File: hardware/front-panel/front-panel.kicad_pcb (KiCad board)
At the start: 2 copper layers, 71.1 x 128.9 mm, 0 parts

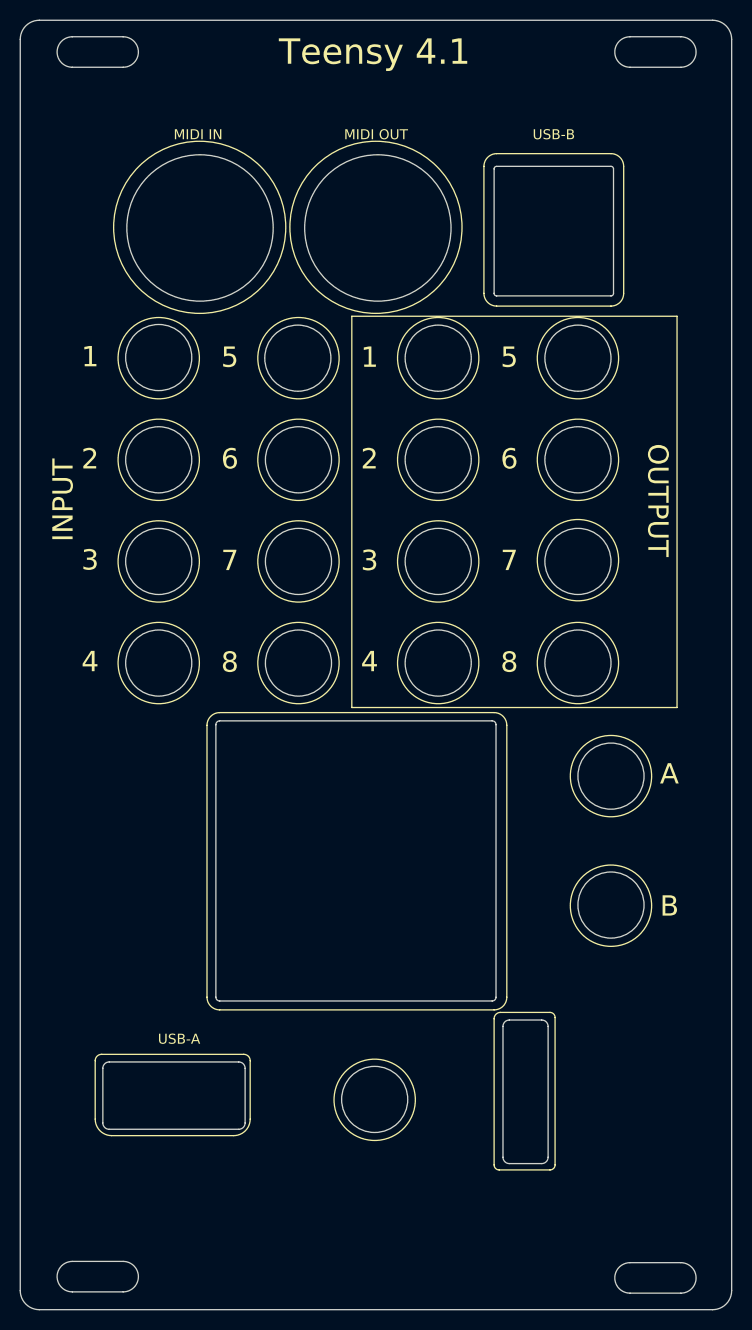
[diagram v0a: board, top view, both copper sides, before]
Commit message: schematic: fix ad7606 pin 8 (range select) from tied to gnd via res, to tied to 3v3 via resistor
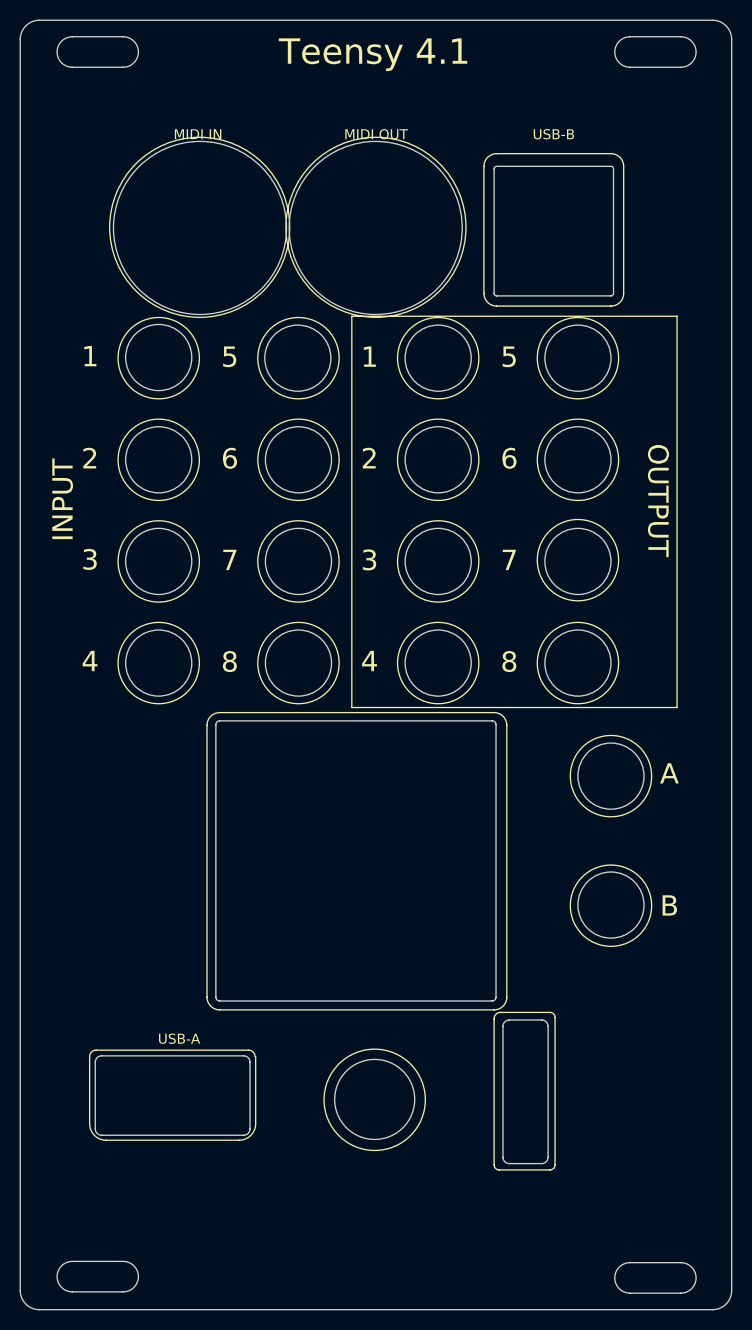
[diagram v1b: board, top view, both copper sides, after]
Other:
- outline, holes or cut-outs redrawn
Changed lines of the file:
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@@
     (uvia_drill 0.1)
   )
-  (gr_poly (pts (xy 77.724 82.042) (xy 45.212 82.042) (xy 45.212 42.926) (xy 77.724 42.926)) (layer F.Mask) (width 0.1))
+  (gr_poly (pts (xy 77.724 82.042) (xy 45.212 82.042) (xy 45.212 61.4) (xy 45.212 42.926) (xy 77.724 42.926)) (layer F.Mask) (width 0.1))
   (gr_line (start 77.724 82.042) (end 77.724 42.926) (layer F.SilkS) (width 0.12))
   (gr_line (start 45.212 82.042) (end 77.724 82.042) (layer F.SilkS) (width 0.12))
@@
   (gr_line (start 60.071 112.522) (end 65.024 112.522) (layer F.SilkS) (width 0.12))
   (gr_line (start 59.436 127.762) (end 59.436 113.157) (layer F.SilkS) (width 0.12))
-  (gr_arc (start 34.417 117.348) (end 35.052 117.348) (angle -90) (layer F.SilkS) (width 0.12))
-  (gr_arc (start 20.193 117.348) (end 20.193 116.713) (angle -90) (layer F.SilkS) (width 0.12))
-  (gr_arc (start 21.209 123.19) (end 19.558 123.19) (angle -90) (layer F.SilkS) (width 0.12))
-  (gr_arc (start 33.401 123.19) (end 33.401 124.841) (angle -90) (layer F.SilkS) (width 0.12))
-  (gr_line (start 21.209 124.841) (end 33.401 124.841) (layer F.SilkS) (width 0.12))
-  (gr_line (start 35.052 123.19) (end 35.052 117.348) (layer F.SilkS) (width 0.12))
-  (gr_line (start 19.558 123.19) (end 19.558 117.348) (layer F.SilkS) (width 0.12))
-  (gr_line (start 20.193 116.713) (end 34.417 116.713) (layer F.SilkS) (width 0.12))
-  (gr_circle (center 47.498 121.2596) (end 51.562 121.2596) (layer F.SilkS) (width 0.12))
+  (gr_arc (start 34.9 116.935) (end 35.535 116.935) (angle -90) (layer F.SilkS) (width 0.12))
+  (gr_arc (start 19.635 116.935) (end 19.635 116.3) (angle -90) (layer F.SilkS) (width 0.12))
+  (gr_arc (start 20.651 123.649) (end 19 123.649) (angle -90) (layer F.SilkS) (width 0.12))
+  (gr_arc (start 33.949 123.649) (end 33.949 125.3) (angle -90) (layer F.SilkS) (width 0.12))
+  (gr_line (start 20.651 125.3) (end 33.949 125.3) (layer F.SilkS) (width 0.12))
+  (gr_line (start 35.6 123.649) (end 35.6 116.935) (layer F.SilkS) (width 0.12))
+  (gr_line (start 19 123.649) (end 19 116.935) (layer F.SilkS) (width 0.12))
+  (gr_line (start 19.635 116.3) (end 34.9 116.3) (layer F.SilkS) (width 0.12))
+  (gr_circle (center 47.498 121.2596) (end 52.562 121.2596) (layer F.SilkS) (width 0.12))
   (gr_line (start 30.734 110.998) (end 30.734 83.82) (layer F.SilkS) (width 0.12))
   (gr_line (start 59.436 112.268) (end 32.004 112.268) (layer F.SilkS) (width 0.12))
   (gr_line (start 60.706 83.82) (end 60.706 110.998) (layer F.SilkS) (width 0.12))
   (gr_line (start 32.004 82.55) (end 59.436 82.55) (layer F.SilkS) (width 0.12))
-  (gr_circle (center 47.625 34.036) (end 48.895 42.545) (layer F.SilkS) (width 0.12))
-  (gr_circle (center 30.004746 34.036) (end 31.274746 42.545) (layer F.SilkS) (width 0.12))
+  (gr_circle (center 47.625 34.036) (end 56.625 34.036) (layer F.SilkS) (width 0.12))
+  (gr_circle (center 30.004746 34.036) (end 39.004746 34.036) (layer F.SilkS) (width 0.12))
   (gr_circle (center 67.818 47.117) (end 71.882 47.117) (layer F.SilkS) (width 0.12))
   (gr_circle (center 53.848 47.117) (end 57.912 47.117) (layer F.SilkS) (width 0.12))
@@
   (gr_line (start 54.2281 124.889) (end 54.2385 124.895) (layer Cmts.User) (width 0.2))
   (gr_line (start 54.2168 124.886) (end 54.2281 124.889) (layer Cmts.User) (width 0.2))
-  (gr_circle (center 47.8155 34.0995) (end 48.26 41.402) (layer Edge.Cuts) (width 0.05))
-  (gr_circle (center 30.0355 34.0995) (end 30.48 41.402) (layer Edge.Cuts) (width 0.05))
+  (gr_circle (center 47.6 34.0995) (end 56.25 34.0995) (layer Edge.Cuts) (width 0.05))
+  (gr_circle (center 30.0355 34.0995) (end 38.6855 34.0995) (layer Edge.Cuts) (width 0.05))
   (gr_circle (center 71.12 101.7905) (end 71.247 105.0925) (layer Edge.Cuts) (width 0.05))
   (gr_circle (center 71.12 88.9) (end 71.247 92.202) (layer Edge.Cuts) (width 0.05))
@@
   (gr_circle (center 39.8145 47.117) (end 39.9415 50.419) (layer Edge.Cuts) (width 0.05))
   (gr_circle (center 25.908 47.0535) (end 26.035 50.3555) (layer Edge.Cuts) (width 0.05))
-  (gr_arc (start 20.955 123.571) (end 20.32 123.571) (angle -90) (layer Edge.Cuts) (width 0.05))
-  (gr_arc (start 33.909 123.571) (end 33.909 124.206) (angle -90) (layer Edge.Cuts) (width 0.05))
-  (gr_arc (start 33.909 118.11) (end 34.544 118.11) (angle -90) (layer Edge.Cuts) (width 0.05))
-  (gr_arc (start 20.955 118.11) (end 20.955 117.475) (angle -90) (layer Edge.Cuts) (width 0.05))
-  (gr_line (start 20.955 117.475) (end 33.909 117.475) (layer Edge.Cuts) (width 0.05))
-  (gr_line (start 34.544 118.11) (end 34.544 123.571) (layer Edge.Cuts) (width 0.05))
-  (gr_line (start 20.955 124.206) (end 33.909 124.206) (layer Edge.Cuts) (width 0.05))
-  (gr_line (start 20.32 118.11) (end 20.32 123.571) (layer Edge.Cuts) (width 0.05))
+  (gr_arc (start 20.2 124.165) (end 19.565 124.165) (angle -90) (layer Edge.Cuts) (width 0.05))
+  (gr_arc (start 34.4 124.165) (end 34.4 124.8) (angle -90) (layer Edge.Cuts) (width 0.05))
+  (gr_arc (start 34.4 117.5) (end 35.035 117.5) (angle -90) (layer Edge.Cuts) (width 0.05))
+  (gr_arc (start 20.2 117.5) (end 20.2 116.865) (angle -90) (layer Edge.Cuts) (width 0.05))
+  (gr_line (start 20.2 116.865) (end 34.4 116.865) (layer Edge.Cuts) (width 0.05))
+  (gr_line (start 35.035 117.5) (end 35.035 124.165) (layer Edge.Cuts) (width 0.05))
+  (gr_line (start 20.2 124.8) (end 34.4 124.8) (layer Edge.Cuts) (width 0.05))
+  (gr_line (start 19.565 117.5) (end 19.565 124.165) (layer Edge.Cuts) (width 0.05))
   (gr_arc (start 64.1985 127) (end 64.1985 127.635) (angle -90) (layer Edge.Cuts) (width 0.05))
   (gr_arc (start 60.96 127) (end 60.325 127) (angle -90) (layer Edge.Cuts) (width 0.05))
@@
   (gr_line (start 60.96 127.635) (end 64.1985 127.635) (layer Edge.Cuts) (width 0.05))
   (gr_line (start 60.325 113.919) (end 60.325 127) (layer Edge.Cuts) (width 0.05))
-  (gr_circle (center 47.498 121.2215) (end 47.625 124.5235) (layer Edge.Cuts) (width 0.05))
+  (gr_circle (center 47.498 121.2215) (end 51.498 121.2215) (layer Edge.Cuts) (width 0.05))
   (gr_arc (start 17.272 16.51) (end 17.272 14.986) (angle -180) (layer Edge.Cuts) (width 0.05))
   (gr_line (start 17.272 18.034) (end 22.352 18.034) (layer Edge.Cuts) (width 0.05))
